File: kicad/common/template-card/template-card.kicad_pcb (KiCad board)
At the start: 2 copper layers, 38 x 64 mm, 7 parts, among them J1 Conn_01x06_Pin, J2 Conn_01x06_Pin, U1 THVD1450DR, U2 STM32C011F4Px

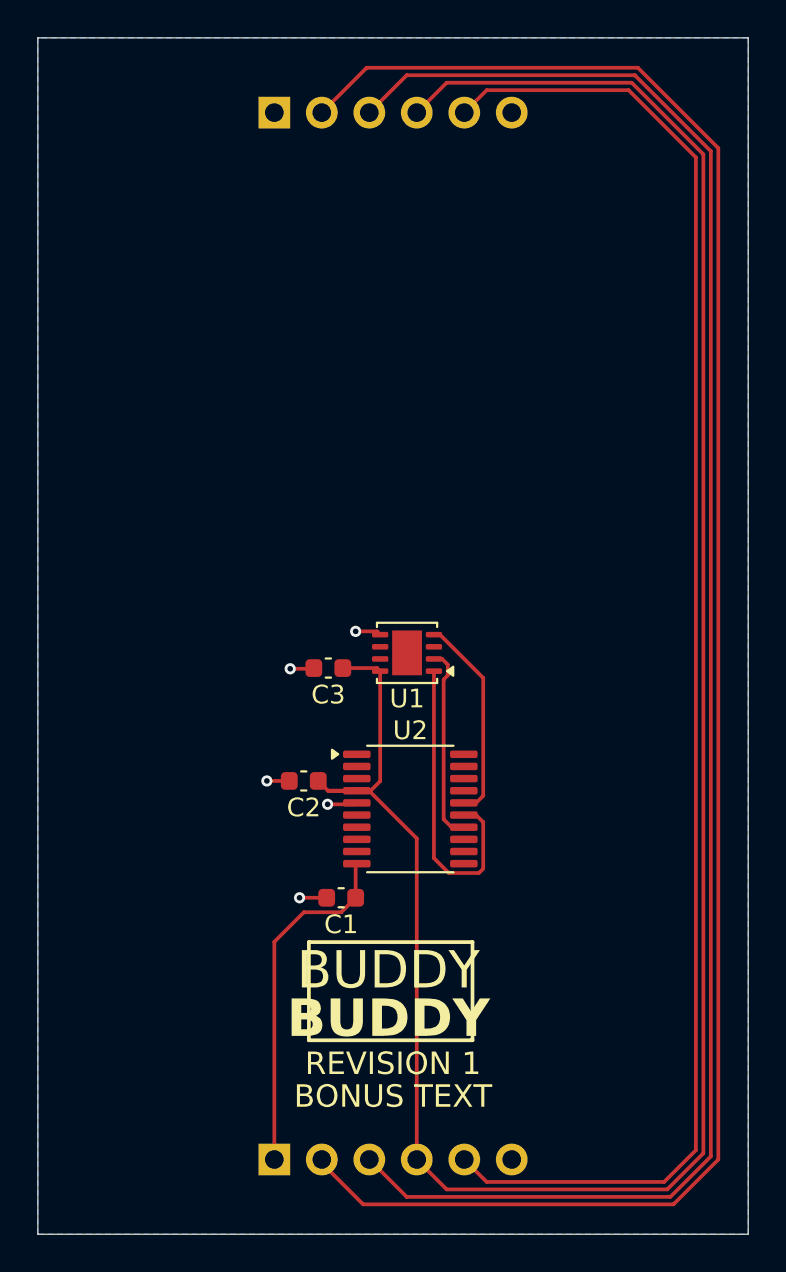
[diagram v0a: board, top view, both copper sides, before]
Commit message: Add card template and knob card
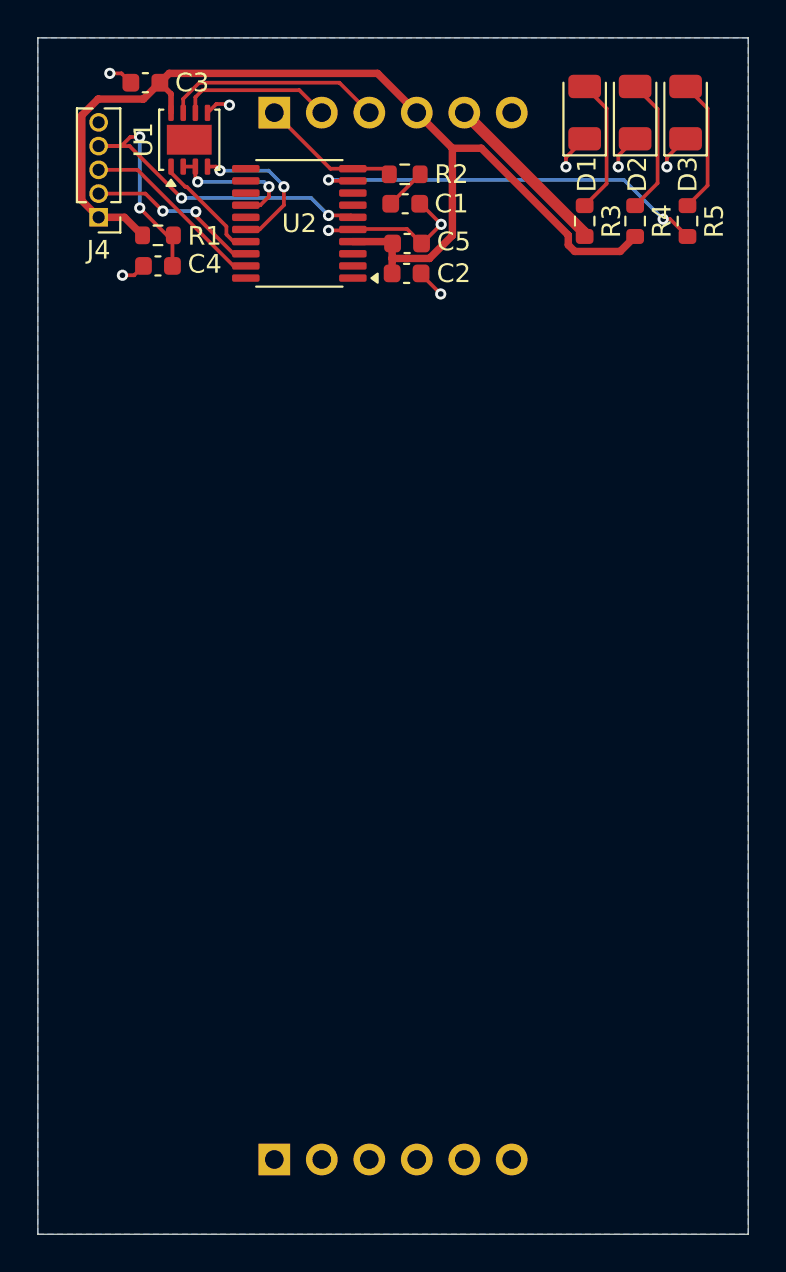
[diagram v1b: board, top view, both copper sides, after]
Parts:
- added C4: 100n, Capacitor_SMD:C_0603_1608Metric, F.Cu at (128.7, 65.7)
- added C5: 1u, Capacitor_SMD:C_0603_1608Metric, F.Cu at (142.0, 64.5)
- added D1: LED, LED_SMD:LED_1206_3216Metric, F.Cu at (151.5, 57.5)
- added D2: LED, LED_SMD:LED_1206_3216Metric, F.Cu at (154.2, 57.5)
- added D3: LED, LED_SMD:LED_1206_3216Metric, F.Cu at (156.9, 57.5)
- added J4: Conn_01x05, Connector_PinHeader_1.27mm:PinHeader_1x05_P1.27mm_Vertical, F.Cu at (125.5, 63.1)
- added R1: 10K, Resistor_SMD:R_0603_1608Metric, F.Cu at (128.7, 64.1)
- added R2: 1K, Resistor_SMD:R_0603_1608Metric, F.Cu at (141.9, 60.8)
- added R3: 1K, Resistor_SMD:R_0603_1608Metric, F.Cu at (151.5, 63.3)
- added R4: 1K, Resistor_SMD:R_0603_1608Metric, F.Cu at (154.2, 63.3)
- added R5: 1K, Resistor_SMD:R_0603_1608Metric, F.Cu at (157.0, 63.3)
- C1, C2: value C -> 100n
- moved C1 37.3 mm to (141.9, 62.4), turned to 0 degrees
- moved C3 32.8 mm to (128.0, 55.9)
- moved U2 31.9 mm to (136.2, 63.4), turned to 180 degrees
- moved U1 29.8 mm to (130.3, 59.0), turned to 90 degrees
- moved C2 27.7 mm to (142.0, 66.1), turned to 0 degrees
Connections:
- C1 pad 1: SLOT -> Net-(C1-Pad1)
- U1 pad 6: BUS_A -> BUS A
- U1 pad 7: BUS_B -> BUS B
- U2 pad 15: BUS_RX -> unconnected-(U2-PA8-Pad15)
- U2 pad 17: unconnected-(U2-PA10/PA12-Pad17) -> BUS_RX
- U2 pad 18: unconnected-(U2-PA13-Pad18) -> SWDIO
- U2 pad 19: unconnected-(U2-PA14-Pad19) -> SWCLK
- U2 pad 6: unconnected-(U2-PF2-Pad6) -> NRST
- U2 pad 9: unconnected-(U2-PA2-Pad9) -> PA2
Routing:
- net BUS A: track 101.4 -> 8.25 mm
- net BUS B: track 94.5 -> 11.7 mm
- net +5V: track 81.1 -> 9.29 mm
- net +3V3: track 122.5 -> 57.7 mm
- net NRST: track 0.00 -> 25.4 mm, vias 0 -> 4
- net PA2: track 0.00 -> 21.8 mm, vias 0 -> 2
- net GND: track 6.91 -> 19.7 mm, vias 5 -> 9
- net SLOT: track 18.8 -> 7.52 mm
- net BUS_RX: track 16.8 -> 6.10 mm
- net SWCLK: track 0.00 -> 10.0 mm
- net SWDIO: track 0.00 -> 9.34 mm, vias 0 -> 2
- net Net-(D2-A): track 0.00 -> 7.37 mm
- net Net-(D1-A): track 0.00 -> 7.35 mm
- net Net-(D3-A): track 0.00 -> 7.31 mm
- net BUS_EN: track 10.5 -> 7.39 mm, vias 0 -> 2
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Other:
- board text added: "REVISION 1 MODEL NO."
- board text removed: "BONUS TEXT"
- board text removed: "REVISION 1"
